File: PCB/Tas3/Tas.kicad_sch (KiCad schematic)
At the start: 36 parts, among them J1 Shelly 1, J2 Conn_01x07, J3 USB-C, Q1 PMF170XP,115, Q2 2N7002BKS, U1 MD8942, U2 Barcode, U3 CH340X

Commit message: Better rails
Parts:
- removed FID1, FID2, FID3, FID4, FID5, FID6, FID7, FID8: Fiducial, Fiducial:Fiducial_1mm_Mask2mm, symbol Mechanical:Fiducial
- added PCB1: 70x70, RevK:PCB7070, symbol RevK:PCB

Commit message: Revised totally
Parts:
- removed D2: BAV99S, RevK:SOT-363_SC-70-6, symbol Diode:BAV99S
- removed Q1: PMF170XP,115, RevK:SOT-323_SC-70, symbol Device:Q_PMOS_GSD
- removed Q2: 2N7002BKS, RevK:SOT-363_SC-70-6, symbol Transistor_FET:FDG1024NZ
- removed R9: 10k, RevK:R_0402, symbol Device:R
- added U4: ISL89410, RevK:SO-8_3.9x4.9mm_P1.27mm, symbol Driver_FET:EL7202CN
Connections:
- net +3V3: now also U4.6 (V+); no longer R8.2
- net B: now also J1.2 (Pin_2), J2.2 (Pin_2), U4.7 (OUT_A); no longer J1.3 (Pin_3), J2.3 (Pin_3)
- net GND: now also U4.3 (GND); no longer U3.5 (~{CTS})
- net GPIO0: now also U4.2 (IN_A); no longer J1.2 (Pin_2), J2.2 (Pin_2)
- net R: now also D1.3 (K1A2)
- net RST: now also U4.4 (IN_B); no longer D1.3 (K1A2)
- new net: R8.2, U3.5 (~{CTS})
- new net RST+: J1.3 (Pin_3), J2.3 (Pin_3), U4.5 (OUT_B)
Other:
- note added: "GPIO0 is driven as the 4k7 nto CTS is upset by stuff on the shelly RST is driven as it is used to power the Shelly 1 models"
- moved on the sheet: R8

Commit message: VCUT
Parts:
- added V1, V2: ~, RevK:VCUT70, symbol RevK:VCUT
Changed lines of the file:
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@@
+    )
+  )
+  (symbol (lib_id "RevK:VCUT") (at 245.745 175.895 0) (unit 1)
+    (in_bom yes) (on_board yes) (dnp no) (fields_autoplaced)
+    (property "Reference" "V1" (at 245.745 174.625 0)
+      (effects (font (size 1.27 1.27)) hide)
+    )
+    (property "Value" "~" (at 245.745 175.895 0)
+      (effects (font (size 1.27 1.27)))
+    )
+    (property "Footprint" "RevK:VCUT70" (at 245.745 177.165 0)
+      (effects (font (size 1.27 1.27)) hide)
+    )
+    (property "Datasheet" "" (at 245.745 175.895 0)
+      (effects (font (size 1.27 1.27)) hide)
+    )
+    (instances
+      (project "Tas"
+        (path "/42713045-fffd-4b2d-ae1e-7232d705fb12"
+          (reference "V1") (unit 1)
+        )
+      )
+      (project "Reference"
+        (path "/825c70b0-4860-42b7-97dc-86bfa46e06fd"
+          (reference "V1") (unit 1)
+        )
+      )
+    )
+  )
+  (symbol (lib_id "RevK:VCUT") (at 245.745 169.545 0) (unit 1)
+    (in_bom yes) (on_board yes) (dnp no) (fields_autoplaced)
+    (property "Reference" "V2" (at 245.745 168.275 0)
+      (effects (font (size 1.27 1.27)) hide)
+    )
+    (property "Value" "~" (at 245.745 169.545 0)
+      (effects (font (size 1.27 1.27)))
+    )
+    (property "Footprint" "RevK:VCUT70" (at 245.745 170.815 0)
+      (effects (font (size 1.27 1.27)) hide)
+    )
+    (property "Datasheet" "" (at 245.745 169.545 0)
+      (effects (font (size 1.27 1.27)) hide)
+    )
+    (instances
+      (project "Tas"
+        (path "/42713045-fffd-4b2d-ae1e-7232d705fb12"
+          (reference "V2") (unit 1)
+        )
+      )
+      (project "Reference"
+        (path "/825c70b0-4860-42b7-97dc-86bfa46e06fd"
+          (reference "V1") (unit 1)
+        )
+      )
     )
   )

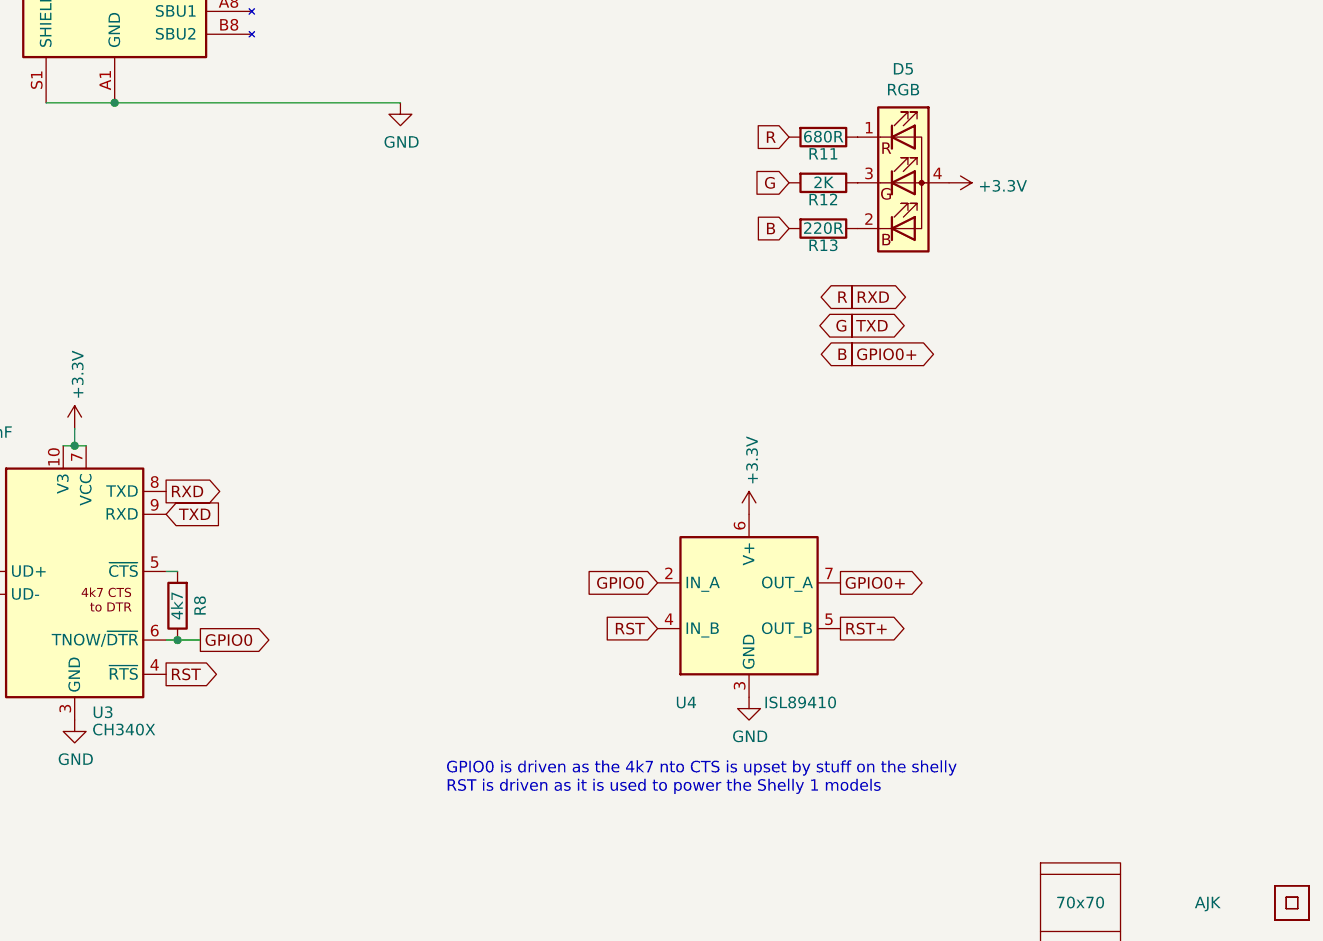
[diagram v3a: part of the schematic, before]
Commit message: Swapped connector to top for single sided assembly
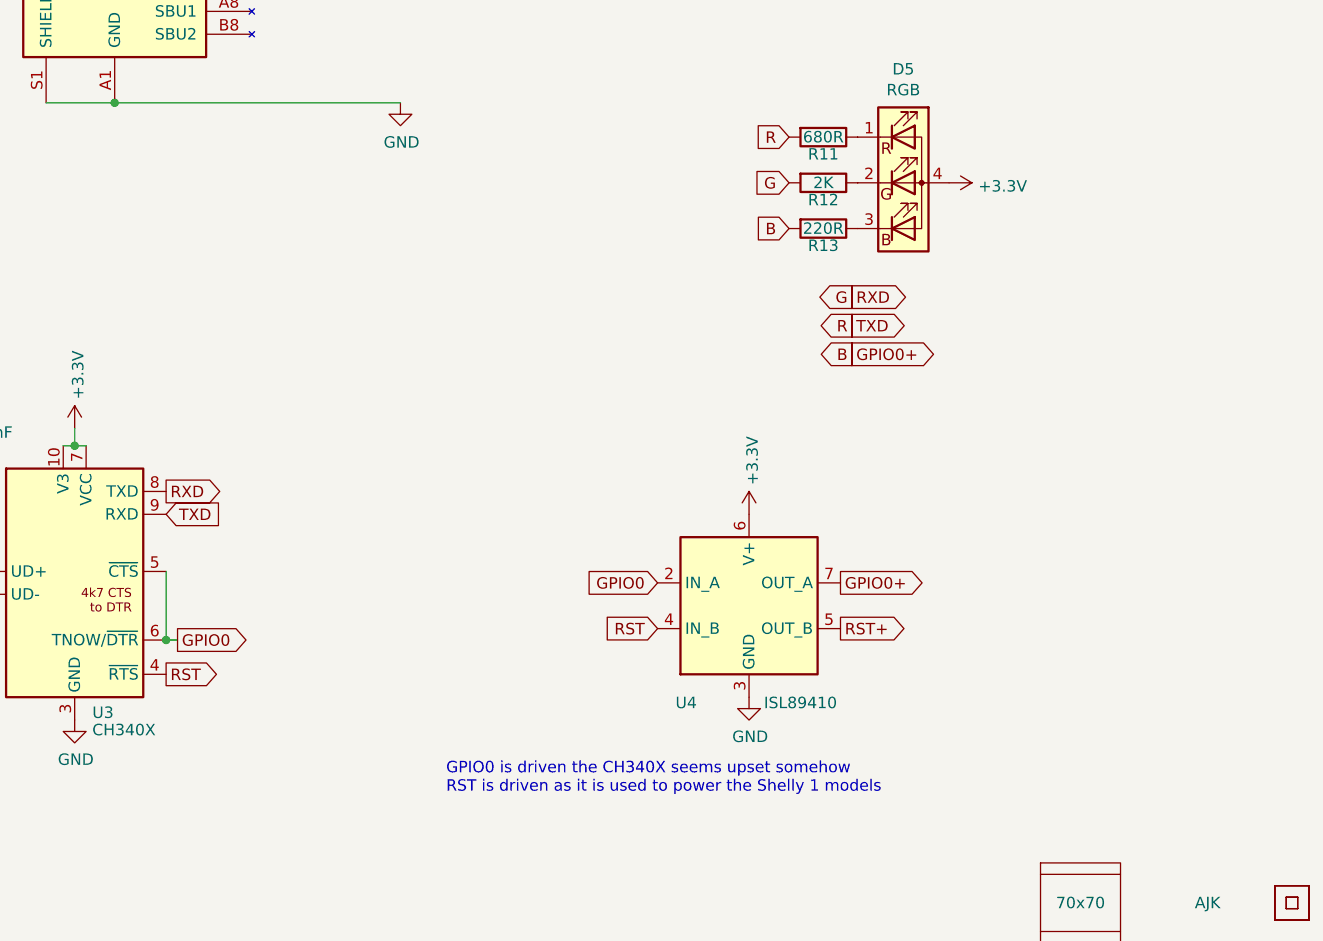
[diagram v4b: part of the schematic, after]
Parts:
- removed R8: 4k7, RevK:R_0402, symbol Device:R
- D5: symbol Device:LED_RBGA -> Device:LED_RGBA
- V1, V2: now left out of the parts list
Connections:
- net G: now also D1.3 (K1A2), J1.4 (Pin_4), J2.5 (Pin_5), U3.8 (TXD); no longer D1.6 (K3A4), J1.5 (Pin_5), J2.6 (Pin_6), U3.9 (RXD)
- net GPIO0: now also U3.5 (~{CTS})
- net R: now also D1.6 (K3A4), J1.5 (Pin_5), J2.6 (Pin_6), U3.9 (RXD); no longer D1.3 (K1A2), J1.4 (Pin_4), J2.5 (Pin_5), U3.8 (TXD)
- net at R12.1: now also D5.2 (GK); no longer D5.3 (GK)
- net at R13.1: now also D5.3 (BK); no longer D5.2 (BK)
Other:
- note added: "GPIO0 is driven the CH340X seems upset somehow RST is driven as it is used to power the Shelly 1 models"
- note removed: "GPIO0 is driven as the 4k7 nto CTS is upset by stuff on the shelly RST is driven as it is used to power the Shelly 1 models"
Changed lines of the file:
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@@
   (junction (at 133.985 121.92) (diameter 0) (color 0 0 0 0)
   )
-  (junction (at 145.415 143.51) (diameter 0) (color 0 0 0 0)
+  (junction (at 144.145 143.51) (diameter 0) (color 0 0 0 0)
   )
   (junction (at 163.83 52.07) (diameter 0) (color 0 0 0 0)
@@
     (stroke (width 0) (type default))
   )
-  (wire (pts (xy 144.145 135.89) (xy 145.415 135.89))
-    (stroke (width 0) (type default))
-  )
   (wire (pts (xy 153.67 50.8) (xy 156.21 50.8))
     (stroke (width 0) (type default))
   )
+  (wire (pts (xy 144.145 135.89) (xy 144.145 143.51))
+    (stroke (width 0) (type default))
+  )
   (wire (pts (xy 138.43 83.82) (xy 170.18 83.82))
     (stroke (width 0) (type default))
@@
     (stroke (width 0) (type default))
   )
-  (wire (pts (xy 145.415 143.51) (xy 147.955 143.51))
-    (stroke (width 0) (type default))
-  )
-  (text "GPIO0 is driven as the 4k7 nto CTS is upset by stuff on the shelly\nRST is driven as it is used to power the Shelly 1 models"
+  (text "GPIO0 is driven the CH340X seems upset somehow\nRST is driven as it is used to power the Shelly 1 models"
     (at 175.26 160.655 0)
     (effects (font (size 1.27 1.27)) (justify left bottom))
@@
     )
   )
-  (global_label "R" (shape output) (at 220.345 105.41 180) (fields_autoplaced)
-    (effects (font (size 1.27 1.27)) (justify right))
-    (property "Intersheetrefs" "${INTERSHEET_REFS}" (at 216.8234 105.41 0)
+  (global_label "R" (shape output) (at 220.345 108.585 180) (fields_autoplaced)
+    (effects (font (size 1.27 1.27)) (justify right))
+    (property "Intersheetrefs" "${INTERSHEET_REFS}" (at 216.8234 108.585 0)
       (effects (font (size 1.27 1.27)) (justify right) hide)
     )
@@
     )
   )
-  (global_label "GPIO0" (shape output) (at 147.955 143.51 0) (fields_autoplaced)
+  (global_label "GPIO0" (shape output) (at 145.415 143.51 0) (fields_autoplaced)
     (effects (font (size 1.27 1.27)) (justify left))
-    (property "Intersheetrefs" "${INTERSHEET_REFS}" (at 155.964 143.4306 0)
+    (property "Intersheetrefs" "${INTERSHEET_REFS}" (at 153.424 143.4306 0)
       (effects (font (size 1.27 1.27)) (justify left) hide)
     )
@@
     )
   )
-  (global_label "G" (shape output) (at 220.345 108.585 180) (fields_autoplaced)
-    (effects (font (size 1.27 1.27)) (justify right))
-    (property "Intersheetrefs" "${INTERSHEET_REFS}" (at 216.8234 108.585 0)
+  (global_label "G" (shape output) (at 220.345 105.41 180) (fields_autoplaced)
+    (effects (font (size 1.27 1.27)) (justify right))
+    (property "Intersheetrefs" "${INTERSHEET_REFS}" (at 216.8234 105.41 0)
       (effects (font (size 1.27 1.27)) (justify right) hide)
     )
@@
     )
   )
-  (symbol (lib_id "Device:R") (at 145.415 139.7 180) (unit 1)
-    (in_bom yes) (on_board yes) (dnp no)
-    (property "Reference" "R8" (at 147.955 139.7 90)
-      (effects (font (size 1.27 1.27)))
-    )
-    (property "Value" "4k7" (at 145.415 139.7 90)
-      (effects (font (size 1.27 1.27)))
-    )
-    (property "Footprint" "RevK:R_0402" (at 147.193 139.7 90)
-      (effects (font (size 1.27 1.27)) hide)
-    )
-    (property "Datasheet" "~" (at 145.415 139.7 0)
-      (effects (font (size 1.27 1.27)) hide)
-    )
-    (pin "1")
-    (pin "2")
-    (instances
-      (project "Tas"
-        (path "/42713045-fffd-4b2d-ae1e-7232d705fb12"
-          (reference "R8") (unit 1)
-        )
-      )
-    )
-  )
   (symbol (lib_id "RevK:PCB") (at 245.745 172.72 0) (unit 1)
     (in_bom no) (on_board yes) (dnp no)
@@
   )
   (symbol (lib_id "RevK:VCUT") (at 245.745 175.895 0) (unit 1)
-    (in_bom yes) (on_board yes) (dnp no) (fields_autoplaced)
+    (in_bom no) (on_board yes) (dnp no) (fields_autoplaced)
     (property "Reference" "V1" (at 245.745 174.625 0)
       (effects (font (size 1.27 1.27)) hide)
@@
     )
     (property "Datasheet" "" (at 245.745 175.895 0)
+      (effects (font (size 1.27 1.27)) hide)
+    )
+    (property "Sim.Enable" "0" (at 245.745 175.895 0)
       (effects (font (size 1.27 1.27)) hide)
     )
@@
   )
   (symbol (lib_id "RevK:VCUT") (at 245.745 169.545 0) (unit 1)
-    (in_bom yes) (on_board yes) (dnp no) (fields_autoplaced)
+    (in_bom no) (on_board yes) (dnp no) (fields_autoplaced)
     (property "Reference" "V2" (at 245.745 168.275 0)
       (effects (font (size 1.27 1.27)) hide)
@@
     )
     (property "Datasheet" "" (at 245.745 169.545 0)
+      (effects (font (size 1.27 1.27)) hide)
+    )
+    (property "Sim.Enable" "0" (at 245.745 169.545 0)
       (effects (font (size 1.27 1.27)) hide)
     )
@@
     )
   )
-  (symbol (lib_id "Device:LED_RBGA") (at 226.06 92.71 0) (unit 1)
+  (symbol (lib_id "Device:LED_RGBA") (at 226.06 92.71 0) (unit 1)
     (in_bom yes) (on_board yes) (dnp no)
     (property "Reference" "D5" (at 226.06 80.0862 0)

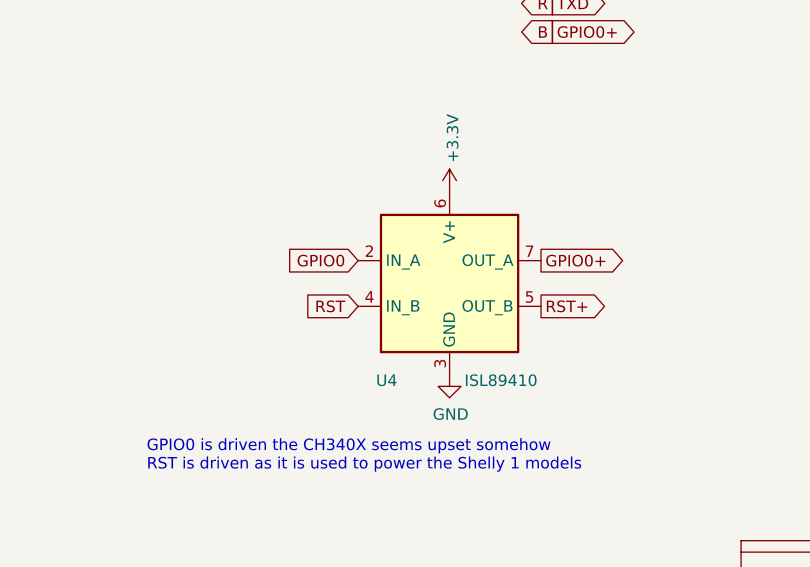
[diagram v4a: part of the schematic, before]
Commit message: Fix output driver
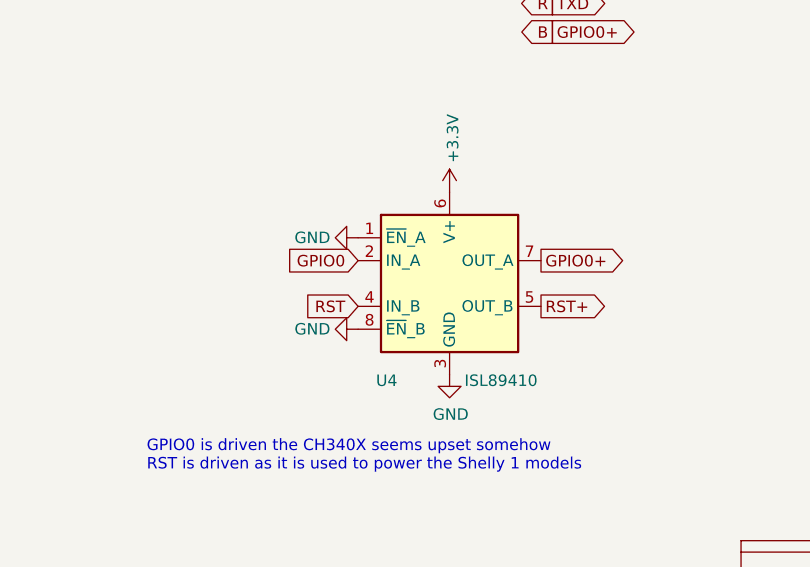
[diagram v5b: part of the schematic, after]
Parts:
- U4: symbol Driver_FET:EL7202CN -> RevK:IVCR2404
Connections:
- net GND: now also U4.1 (~{EN}_A), U4.8 (~{EN}_B)
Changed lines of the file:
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@@
+    )
+  )
+  (symbol (lib_id "power:GND") (at 198.755 144.78 270) (unit 1)
+    (in_bom yes) (on_board yes) (dnp no)
+    (property "Reference" "#PWR08" (at 192.405 144.78 0)
+      (effects (font (size 1.27 1.27)) hide)
+    )
+    (property "Value" "GND" (at 193.675 144.78 90)
+      (effects (font (size 1.27 1.27)))
+    )
+    (property "Footprint" "" (at 198.755 144.78 0)
+      (effects (font (size 1.27 1.27)) hide)
+    )
+    (property "Datasheet" "" (at 198.755 144.78 0)
+      (effects (font (size 1.27 1.27)) hide)
+    )
+    (pin "1")
+    (instances
+      (project "Tas"
+        (path "/42713045-fffd-4b2d-ae1e-7232d705fb12"
+          (reference "#PWR08") (unit 1)
+        )
+      )
     )
   )
@@
     )
   )
-  (symbol (lib_id "Driver_FET:EL7202CN") (at 208.915 139.7 0) (unit 1)
+  (symbol (lib_id "RevK:IVCR2404") (at 208.915 139.7 0) (unit 1)
     (in_bom yes) (on_board yes) (dnp no)
     (property "Reference" "U4" (at 201.93 150.495 0)
@@
         )
       )
+    )
+  )
+  (symbol (lib_id "power:GND") (at 198.755 134.62 270) (unit 1)
+    (in_bom yes) (on_board yes) (dnp no)
+    (property "Reference" "#PWR09" (at 192.405 134.62 0)
+      (effects (font (size 1.27 1.27)) hide)
+    )
+    (property "Value" "GND" (at 193.675 134.62 90)
+      (effects (font (size 1.27 1.27)))
+    )
+    (property "Footprint" "" (at 198.755 134.62 0)
+      (effects (font (size 1.27 1.27)) hide)
+    )
+    (property "Datasheet" "" (at 198.755 134.62 0)
+      (effects (font (size 1.27 1.27)) hide)
+    )
+    (pin "1")
+    (instances
+      (project "Tas"
+        (path "/42713045-fffd-4b2d-ae1e-7232d705fb12"
+          (reference "#PWR09") (unit 1)
+        )
+      )

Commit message: As ordered
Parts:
- removed U4: ISL89410, RevK:SO-8_3.9x4.9mm_P1.27mm, symbol RevK:IVCR2404
- added U4, U5: ZXGD3009E6, RevK:SOT-23-6, symbol Driver_FET:ZXGD3009E6
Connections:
- net +3V3: now also U4.1 (VCC), U5.1 (VCC)
- net B: now also U4.4 (SINK), U4.6 (SOURCE)
- net GND: now also U4.3 (VEE), U5.3 (VEE)
- net GPIO0: now also U4.2 (IN)
- net RST: now also U5.2 (IN)
- net RST+: now also U5.4 (SINK), U5.6 (SOURCE)
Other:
- note added: "Cannot connect GPIO0 directly as internal pulls in shelly upset CH340X"
- note removed: "GPIO0 is driven the CH340X seems upset somehow RST is driven as it is used to power the Shelly 1 models"
- moved on the sheet: D5, R11, R12, R13
